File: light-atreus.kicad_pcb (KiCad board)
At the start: 2 copper layers, 2 parts

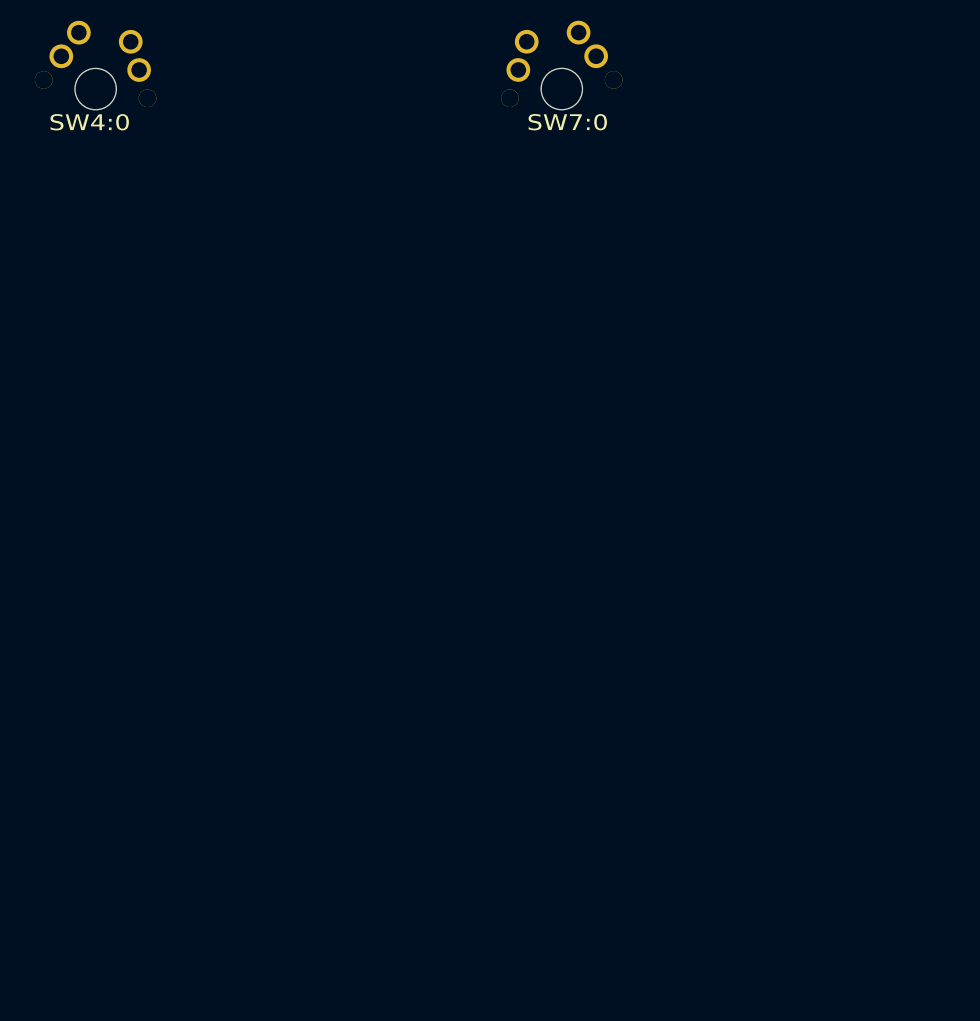
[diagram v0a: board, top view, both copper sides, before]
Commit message: Position mounting holes correctly relative to keys
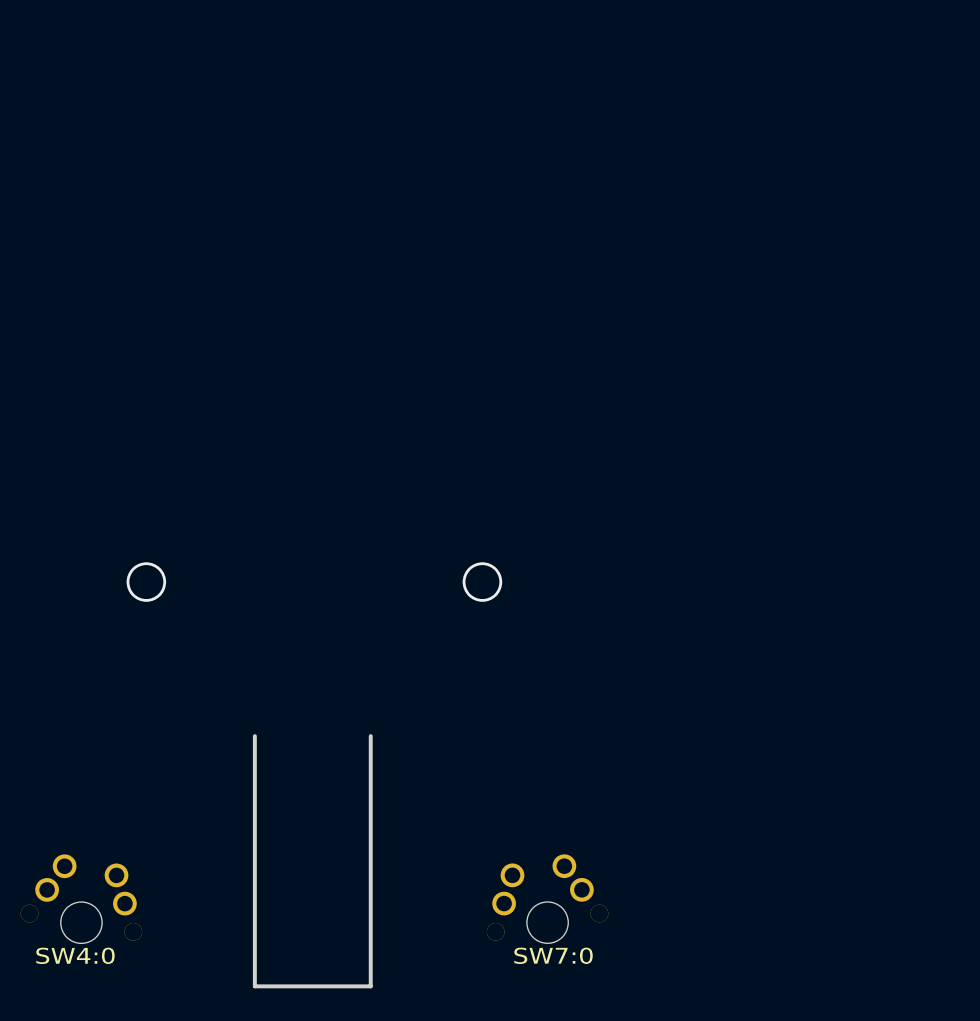
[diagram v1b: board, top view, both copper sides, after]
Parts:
- moved SW4:0 80.4 mm to (110.3, 127.7)
- moved SW7:0 80.4 mm to (155.2, 127.7)
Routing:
- net (no net): vias 0 -> 2
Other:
- board outline added: 11.2 x 24.1 mm
- rule trace_min: 0.2032 -> 0.1778
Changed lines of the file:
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@@
   (general
     (thickness 1.6002)
-    (drawings 5)
-    (tracks 0)
+    (drawings 8)
+    (tracks 2)
     (zones 0)
     (modules 2)
@@
     (zone_clearance 0.508)
     (zone_45_only no)
-    (trace_min 0.2032)
+    (trace_min 0.1778)
     (segment_width 0.381)
     (edge_width 0.381)
@@
     (via_min_size 0.889)
     (via_min_drill 0.508)
+    (user_via 3.81 3.2766)
     (uvia_size 0.508)
     (uvia_drill 0.127)
@@
   )
   (module MX_FLIP locked (layer Front)
-    (at 111.646607 47.329462 350)
+    (at 110.275007 127.720462 350)
     (fp_text reference SW4:0 (at 0 3.302) (layer F.SilkS)
       (effects (font (size 1.524 1.778) (thickness 0.254)))
@@
   )
   (module MX_FLIP locked (layer Front)
-    (at 156.600908 47.323362 10)
+    (at 155.229308 127.714362 10)
     (fp_text reference SW7:0 (at 0 3.302) (layer F.SilkS)
       (effects (font (size 1.524 1.778) (thickness 0.254)))
@@
       (net 4 N-diode-28))
   )
-  (gr_line (start 84 22) (end 128 30) (angle 90) (layer Cmts.User) (width 0.3))
-  (gr_line (start 128 30) (end 128 54) (angle 90) (layer Cmts.User) (width 0.3))
-  (gr_line (start 128 54) (end 140 54) (angle 90) (layer Cmts.User) (width 0.3))
-  (gr_line (start 140 54) (end 140 30) (angle 90) (layer Cmts.User) (width 0.3))
-  (gr_line (start 140 30) (end 185 22) (angle 90) (layer Cmts.User) (width 0.3))
+  (gr_line (start 127 133.858) (end 127 109.728) (layer Edge.Cuts) (width 0.381))
+  (gr_line (start 138.176 133.858) (end 138.176 109.728) (layer Edge.Cuts) (width 0.381))
+  (gr_line (start 127 133.858) (end 138.176 133.858) (layer Edge.Cuts) (width 0.381))
+  (gr_line (start 82.6284 102.391) (end 126.6284 110.391) (angle 90) (layer Cmts.User) (width 0.3))
+  (gr_line (start 126.6284 110.391) (end 126.6284 134.391) (angle 90) (layer Cmts.User) (width 0.3))
+  (gr_line (start 126.6284 134.391) (end 138.6284 134.391) (angle 90) (layer Cmts.User) (width 0.3))
+  (gr_line (start 138.6284 134.391) (end 138.6284 110.391) (angle 90) (layer Cmts.User) (width 0.3))
+  (gr_line (start 138.6284 110.391) (end 183.6284 102.391) (angle 90) (layer Cmts.User) (width 0.3))
+  (via (at 116.5352 94.869) (size 3.81) (drill 3.2766) (layers Front Back) (net 0))
+  (via (at 148.9456 94.869) (size 3.81) (drill 3.2766) (layers Front Back) (net 0))
 )

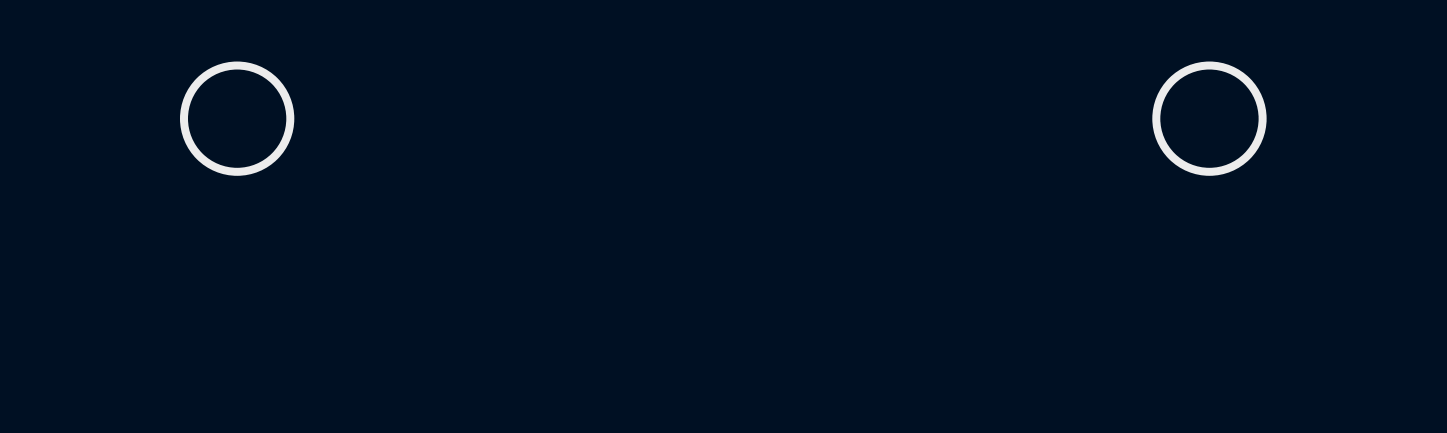
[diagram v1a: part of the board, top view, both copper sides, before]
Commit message: Account for using slightly different reference points
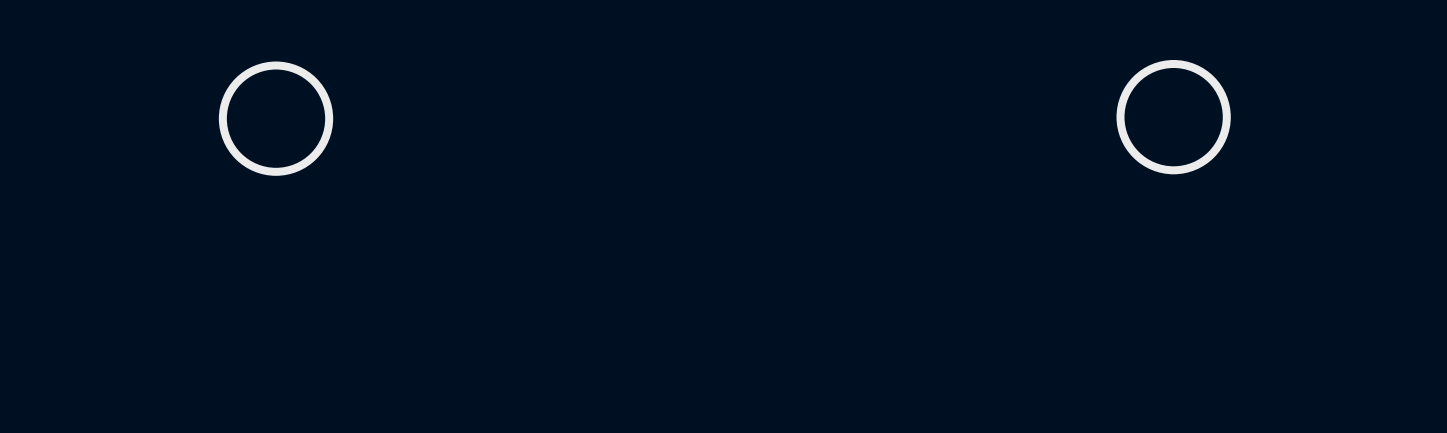
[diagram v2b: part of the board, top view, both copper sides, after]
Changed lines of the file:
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@@
   (gr_line (start 138.6284 134.391) (end 138.6284 110.391) (angle 90) (layer Cmts.User) (width 0.3))
   (gr_line (start 138.6284 110.391) (end 183.6284 102.391) (angle 90) (layer Cmts.User) (width 0.3))
-  (via (at 116.5352 94.869) (size 3.81) (drill 3.2766) (layers Front Back) (net 0))
-  (via (at 148.9456 94.869) (size 3.81) (drill 3.2766) (layers Front Back) (net 0))
+  (via (at 117.8306 94.869) (size 3.81) (drill 3.2766) (layers Front Back) (net 0))
+  (via (at 147.7518 94.8182) (size 3.81) (drill 3.2766) (layers Front Back) (net 0))
 )

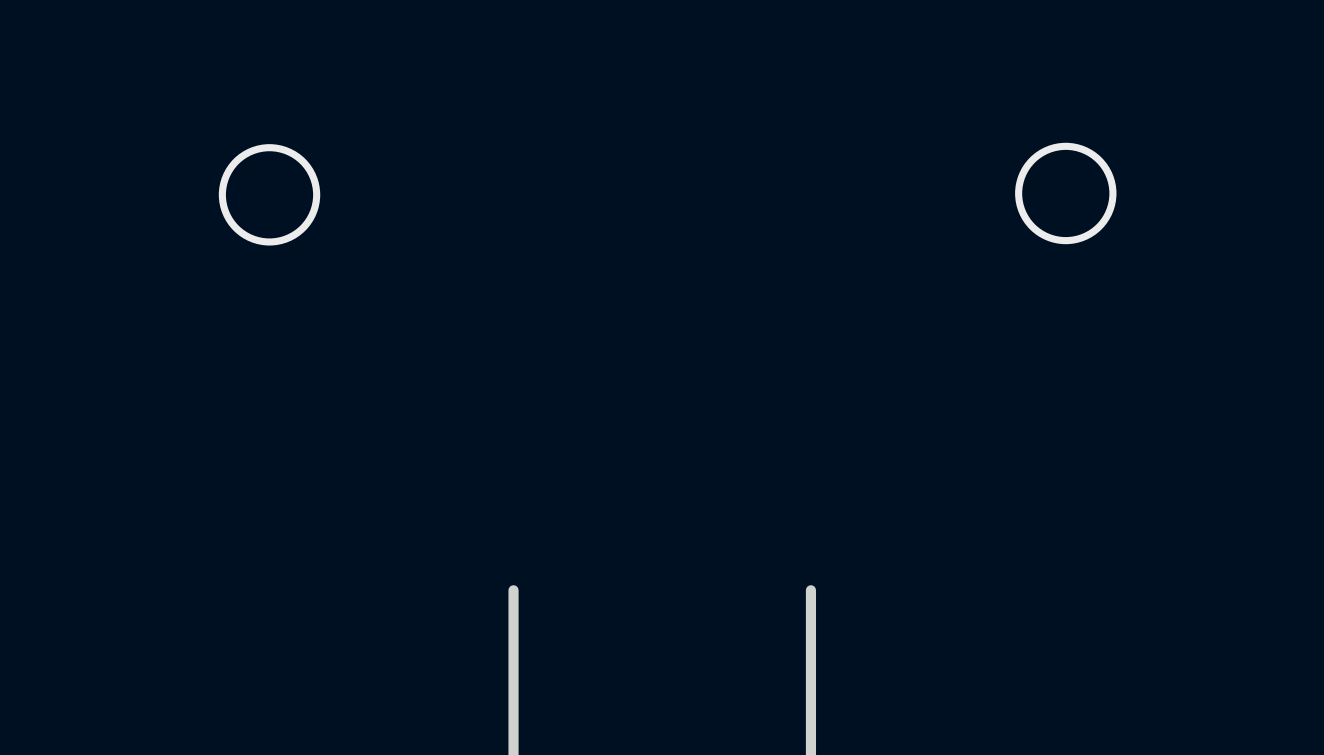
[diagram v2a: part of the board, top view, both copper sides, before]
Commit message: Add actual edge lines
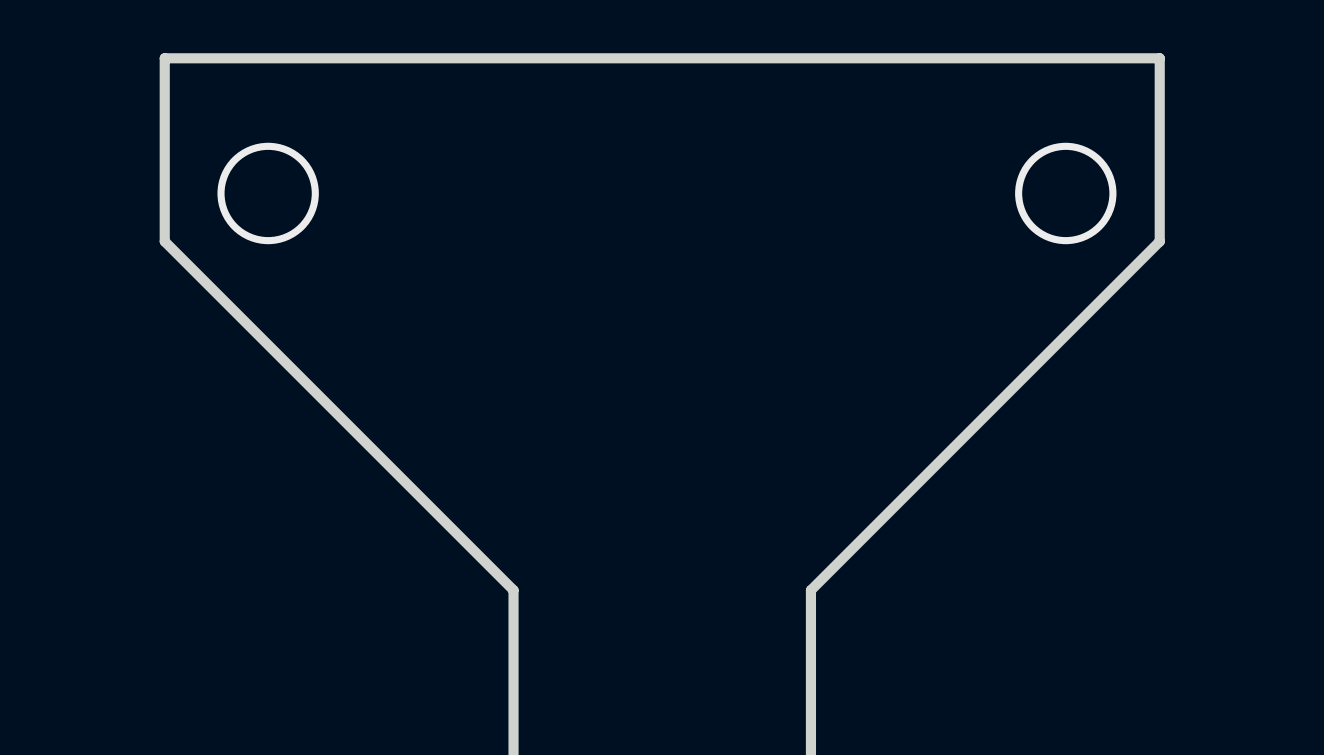
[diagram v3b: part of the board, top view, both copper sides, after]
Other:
- board size 11.2 x 24.1 mm -> 37.4 x 44.1 mm
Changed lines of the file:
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@@
   (general
     (thickness 1.6002)
-    (drawings 8)
+    (drawings 13)
     (tracks 2)
     (zones 0)
@@
       (net 4 N-diode-28))
   )
+  (gr_line (start 151.2824 96.6216) (end 138.176 109.728) (layer Edge.Cuts) (width 0.381))
+  (gr_line (start 113.8936 96.6216) (end 113.8936 89.7382) (layer Edge.Cuts) (width 0.381))
+  (gr_line (start 127 109.728) (end 113.8936 96.6216) (layer Edge.Cuts) (width 0.381))
+  (gr_line (start 151.2824 89.7382) (end 151.2824 96.6216) (layer Edge.Cuts) (width 0.381))
+  (gr_line (start 113.8936 89.7382) (end 151.2824 89.7382) (layer Edge.Cuts) (width 0.381))
   (gr_line (start 127 133.858) (end 127 109.728) (layer Edge.Cuts) (width 0.381))
   (gr_line (start 138.176 133.858) (end 138.176 109.728) (layer Edge.Cuts) (width 0.381))
@@
   (gr_line (start 138.6284 134.391) (end 138.6284 110.391) (angle 90) (layer Cmts.User) (width 0.3))
   (gr_line (start 138.6284 110.391) (end 183.6284 102.391) (angle 90) (layer Cmts.User) (width 0.3))
-  (via (at 117.8306 94.869) (size 3.81) (drill 3.2766) (layers Front Back) (net 0))
+  (via (at 117.7798 94.8182) (size 3.81) (drill 3.2766) (layers Front Back) (net 0))
   (via (at 147.7518 94.8182) (size 3.81) (drill 3.2766) (layers Front Back) (net 0))
 )

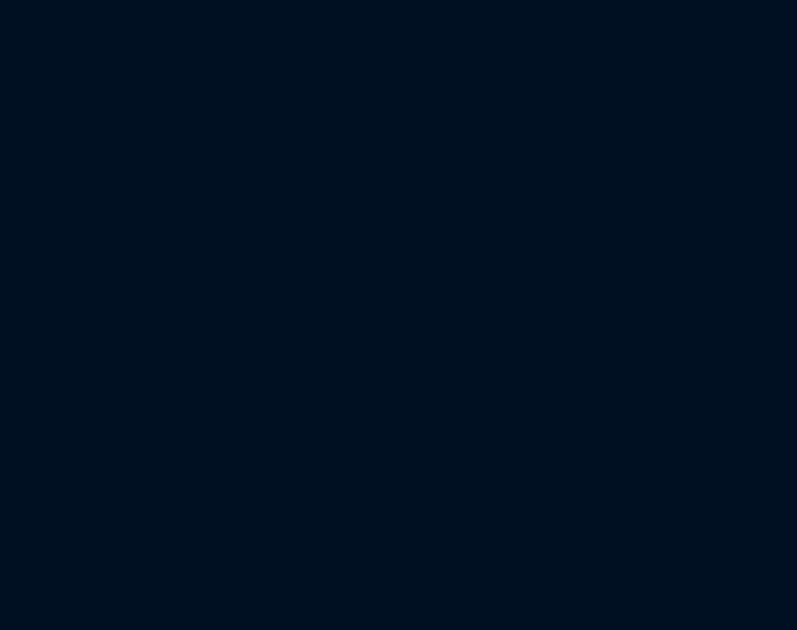
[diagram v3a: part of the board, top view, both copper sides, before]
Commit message: Use banana jack connector pads
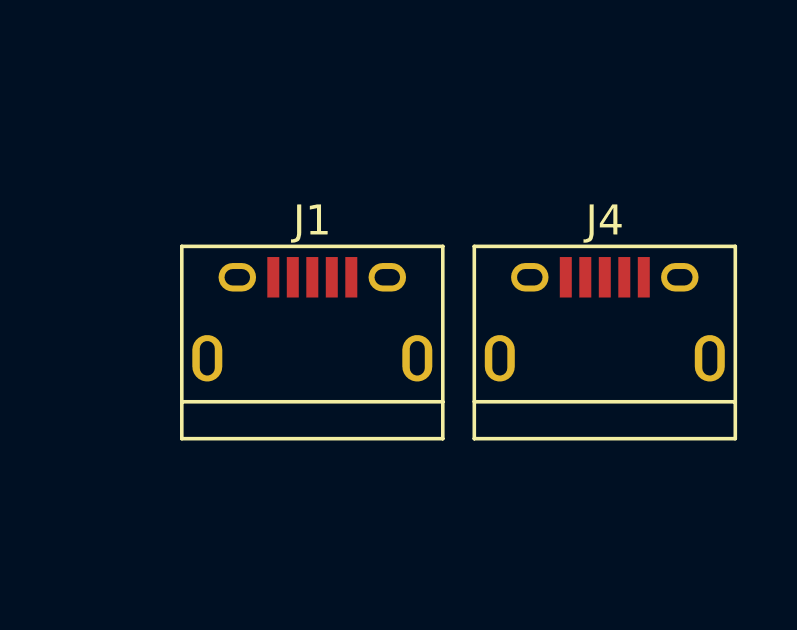
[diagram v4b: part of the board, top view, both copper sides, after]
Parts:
- added J1: USB_OTG, Connectors:USB_Micro-B, F.Cu at (180.7, 121.1)
- added J4: USB_OTG, Connectors:USB_Micro-B, F.Cu at (190.5, 121.1)
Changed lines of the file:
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@@
     (tracks 2)
     (zones 0)
-    (modules 2)
-    (nets 5)
+    (modules 4)
+    (nets 11)
   )
   (page A4)
@@
   (net 3 N-diode-16)
   (net 4 N-diode-28)
+  (net 5 "Net-(J1-Pad6)")
+  (net 6 "Net-(J1-Pad5)")
+  (net 7 "Net-(J1-Pad4)")
+  (net 8 "Net-(J1-Pad3)")
+  (net 9 "Net-(J1-Pad2)")
+  (net 10 "Net-(J1-Pad1)")
   (net_class Default "This is the default net class."
     (clearance 0.254)
@@
     (add_net N-diode-16)
     (add_net N-diode-28)
+    (add_net "Net-(J1-Pad1)")
+    (add_net "Net-(J1-Pad2)")
+    (add_net "Net-(J1-Pad3)")
+    (add_net "Net-(J1-Pad4)")
+    (add_net "Net-(J1-Pad5)")
+    (add_net "Net-(J1-Pad6)")
   )
   (module MX_FLIP locked (layer Front)
@@
       (net 4 N-diode-28))
   )
+  (module Connectors:USB_Micro-B (layer Front)
+    (at 180.723742 121.085187)
+    (descr "Micro USB Type B Receptacle")
+    (tags "USB USB_B USB_micro USB_OTG")
+    (attr smd)
+    (fp_text reference J1 (at 0 -3.24) (layer F.SilkS)
+      (effects (font (size 1 1) (thickness 0.15)))
+    )
+    (fp_text value USB_OTG (at 0 5.01) (layer F.Fab)
+      (effects (font (size 1 1) (thickness 0.15)))
+    )
+    (fp_line (start -4.35 4.03) (end -4.35 -2.38) (layer F.SilkS) (width 0.12))
+    (fp_line (start 4.35 2.8) (end -4.35 2.8) (layer F.SilkS) (width 0.12))
+    (fp_line (start 4.35 -2.38) (end 4.35 4.03) (layer F.SilkS) (width 0.12))
+    (fp_line (start -4.35 -2.38) (end 4.35 -2.38) (layer F.SilkS) (width 0.12))
+    (fp_line (start -4.35 4.03) (end 4.35 4.03) (layer F.SilkS) (width 0.12))
+    (fp_line (start -4.6 4.26) (end -4.6 -2.59) (layer F.CrtYd) (width 0.05))
+    (fp_line (start 4.6 4.26) (end -4.6 4.26) (layer F.CrtYd) (width 0.05))
+    (fp_line (start 4.6 -2.59) (end 4.6 4.26) (layer F.CrtYd) (width 0.05))
+    (fp_line (start -4.6 -2.59) (end 4.6 -2.59) (layer F.CrtYd) (width 0.05))
+    (pad 6 thru_hole oval (at 3.5 1.35 90) (size 1.55 1) (drill oval 1.15 0.5) (layers *.Cu *.Mask)
+      (net 5 "Net-(J1-Pad6)"))
+    (pad 6 thru_hole oval (at -3.5 1.35 90) (size 1.55 1) (drill oval 1.15 0.5) (layers *.Cu *.Mask)
+      (net 5 "Net-(J1-Pad6)"))
+    (pad 6 thru_hole oval (at 2.5 -1.35 90) (size 0.95 1.25) (drill oval 0.55 0.85) (layers *.Cu *.Mask)
+      (net 5 "Net-(J1-Pad6)"))
+    (pad 6 thru_hole oval (at -2.5 -1.35 90) (size 0.95 1.25) (drill oval 0.55 0.85) (layers *.Cu *.Mask)
+      (net 5 "Net-(J1-Pad6)"))
+    (pad 5 smd rect (at 1.3 -1.35 90) (size 1.35 0.4) (layers Front F.Paste F.Mask)
+      (net 6 "Net-(J1-Pad5)"))
+    (pad 4 smd rect (at 0.65 -1.35 90) (size 1.35 0.4) (layers Front F.Paste F.Mask)
+      (net 7 "Net-(J1-Pad4)"))
+    (pad 3 smd rect (at 0 -1.35 90) (size 1.35 0.4) (layers Front F.Paste F.Mask)
+      (net 8 "Net-(J1-Pad3)"))
+    (pad 2 smd rect (at -0.65 -1.35 90) (size 1.35 0.4) (layers Front F.Paste F.Mask)
+      (net 9 "Net-(J1-Pad2)"))
+    (pad 1 smd rect (at -1.3 -1.35 90) (size 1.35 0.4) (layers Front F.Paste F.Mask)
+      (net 10 "Net-(J1-Pad1)"))
+  )
+  (module Connectors:USB_Micro-B (layer Front)
+    (at 190.473742 121.085187)
+    (descr "Micro USB Type B Receptacle")
+    (tags "USB USB_B USB_micro USB_OTG")
+    (attr smd)
+    (fp_text reference J4 (at 0 -3.24) (layer F.SilkS)
+      (effects (font (size 1 1) (thickness 0.15)))
+    )
+    (fp_text value USB_OTG (at 0 5.01) (layer F.Fab)
+      (effects (font (size 1 1) (thickness 0.15)))
+    )
+    (fp_line (start -4.6 -2.59) (end 4.6 -2.59) (layer F.CrtYd) (width 0.05))
+    (fp_line (start 4.6 -2.59) (end 4.6 4.26) (layer F.CrtYd) (width 0.05))
+    (fp_line (start 4.6 4.26) (end -4.6 4.26) (layer F.CrtYd) (width 0.05))
+    (fp_line (start -4.6 4.26) (end -4.6 -2.59) (layer F.CrtYd) (width 0.05))
+    (fp_line (start -4.35 4.03) (end 4.35 4.03) (layer F.SilkS) (width 0.12))
+    (fp_line (start -4.35 -2.38) (end 4.35 -2.38) (layer F.SilkS) (width 0.12))
+    (fp_line (start 4.35 -2.38) (end 4.35 4.03) (layer F.SilkS) (width 0.12))
+    (fp_line (start 4.35 2.8) (end -4.35 2.8) (layer F.SilkS) (width 0.12))
+    (fp_line (start -4.35 4.03) (end -4.35 -2.38) (layer F.SilkS) (width 0.12))
+    (pad 1 smd rect (at -1.3 -1.35 90) (size 1.35 0.4) (layers Front F.Paste F.Mask)
+      (net 10 "Net-(J1-Pad1)"))
+    (pad 2 smd rect (at -0.65 -1.35 90) (size 1.35 0.4) (layers Front F.Paste F.Mask)
+      (net 9 "Net-(J1-Pad2)"))
+    (pad 3 smd rect (at 0 -1.35 90) (size 1.35 0.4) (layers Front F.Paste F.Mask)
+      (net 8 "Net-(J1-Pad3)"))
+    (pad 4 smd rect (at 0.65 -1.35 90) (size 1.35 0.4) (layers Front F.Paste F.Mask)
+      (net 7 "Net-(J1-Pad4)"))
+    (pad 5 smd rect (at 1.3 -1.35 90) (size 1.35 0.4) (layers Front F.Paste F.Mask)
+      (net 6 "Net-(J1-Pad5)"))
+    (pad 6 thru_hole oval (at -2.5 -1.35 90) (size 0.95 1.25) (drill oval 0.55 0.85) (layers *.Cu *.Mask)
+      (net 5 "Net-(J1-Pad6)"))
+    (pad 6 thru_hole oval (at 2.5 -1.35 90) (size 0.95 1.25) (drill oval 0.55 0.85) (layers *.Cu *.Mask)
+      (net 5 "Net-(J1-Pad6)"))
+    (pad 6 thru_hole oval (at -3.5 1.35 90) (size 1.55 1) (drill oval 1.15 0.5) (layers *.Cu *.Mask)
+      (net 5 "Net-(J1-Pad6)"))
+    (pad 6 thru_hole oval (at 3.5 1.35 90) (size 1.55 1) (drill oval 1.15 0.5) (layers *.Cu *.Mask)
+      (net 5 "Net-(J1-Pad6)"))
+  )
   (gr_line (start 151.2824 96.6216) (end 138.176 109.728) (layer Edge.Cuts) (width 0.381))
